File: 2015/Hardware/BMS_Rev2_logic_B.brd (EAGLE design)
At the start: 45.4 x 57.3 mm, 38 parts, among them Q9 MOSFET-NCHANNEL2N7002PW

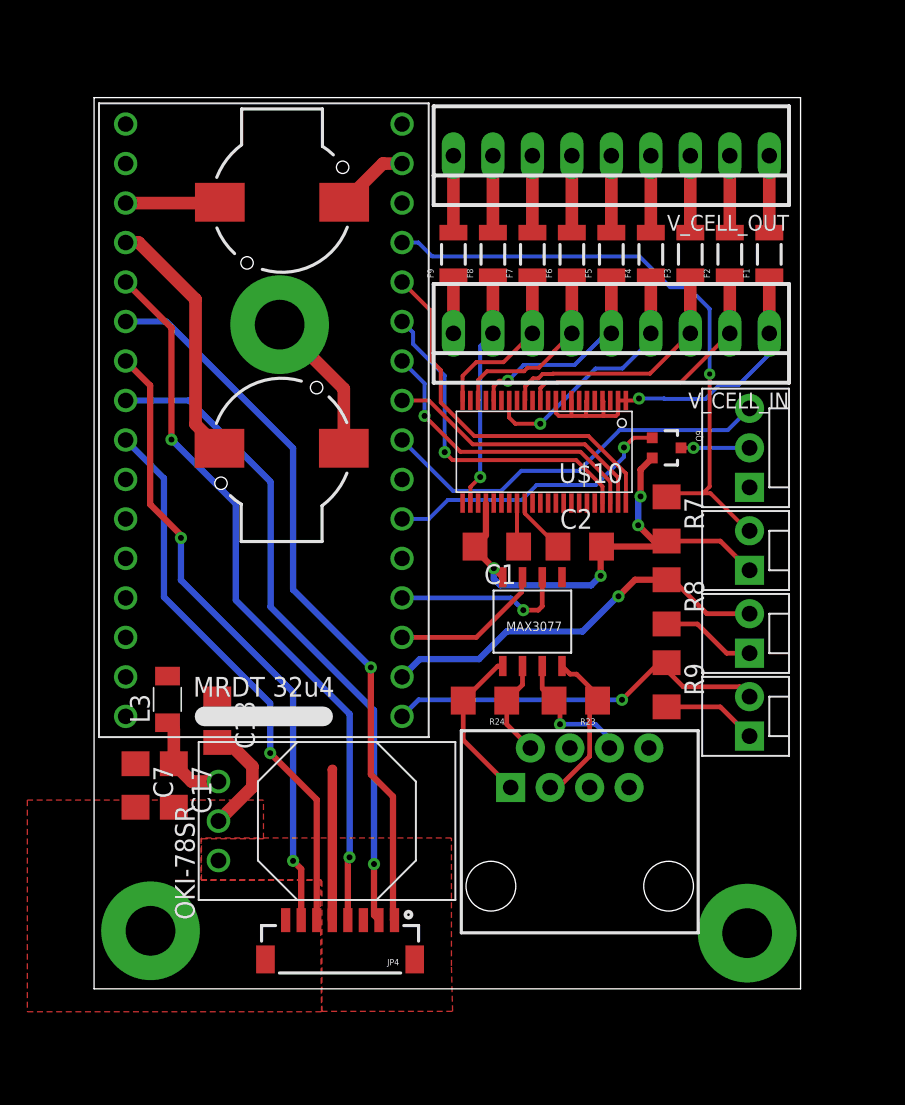
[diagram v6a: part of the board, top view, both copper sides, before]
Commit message: Fixed DRC errors. FreeDFM needs to be run to confirm
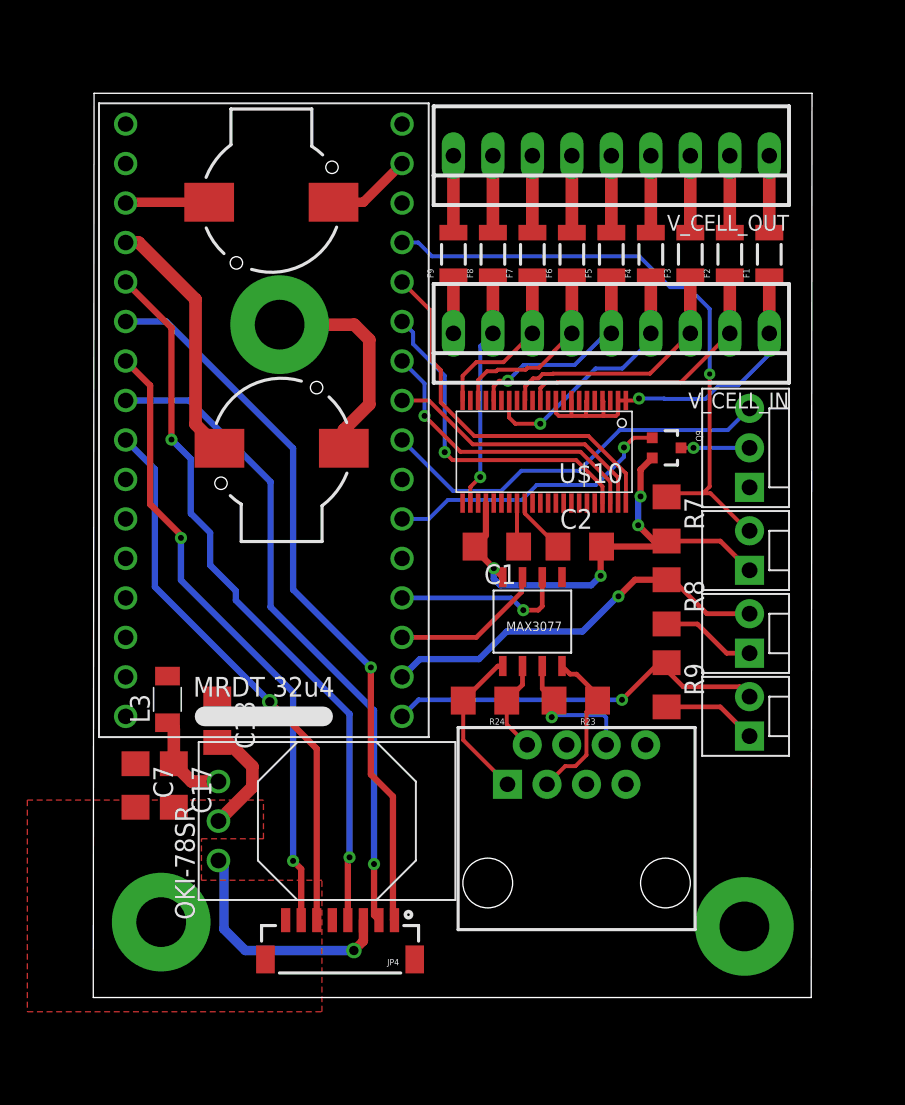
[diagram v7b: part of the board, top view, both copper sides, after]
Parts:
- moved S2 0.88 mm to (4.32, 0.99)
- moved BUZZER_2 0.69 mm to (11.4, 47.3)
- moved S1 0.47 mm to (41.8, 0.71)
- moved U$6 0.29 mm to (31.0, 3.51)
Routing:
- net LOGIC_POWER: track 0.00 -> 15.7 mm, vias 0 -> 1
- net 5V: track 9.71 -> 0.00 mm
- net GND: track 70.7 -> 75.6 mm
- net BUZZ_2: track 6.82 -> 5.39 mm
- net N$10: track 10.6 -> 11.3 mm
- net N$9: track 8.40 -> 9.04 mm
- removed copper zone on layer 1, net LOGIC_POWER
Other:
- board size 45.4 x 57.3 mm -> 46.2 x 58.2 mm
